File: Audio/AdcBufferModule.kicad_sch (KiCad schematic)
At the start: 13 parts

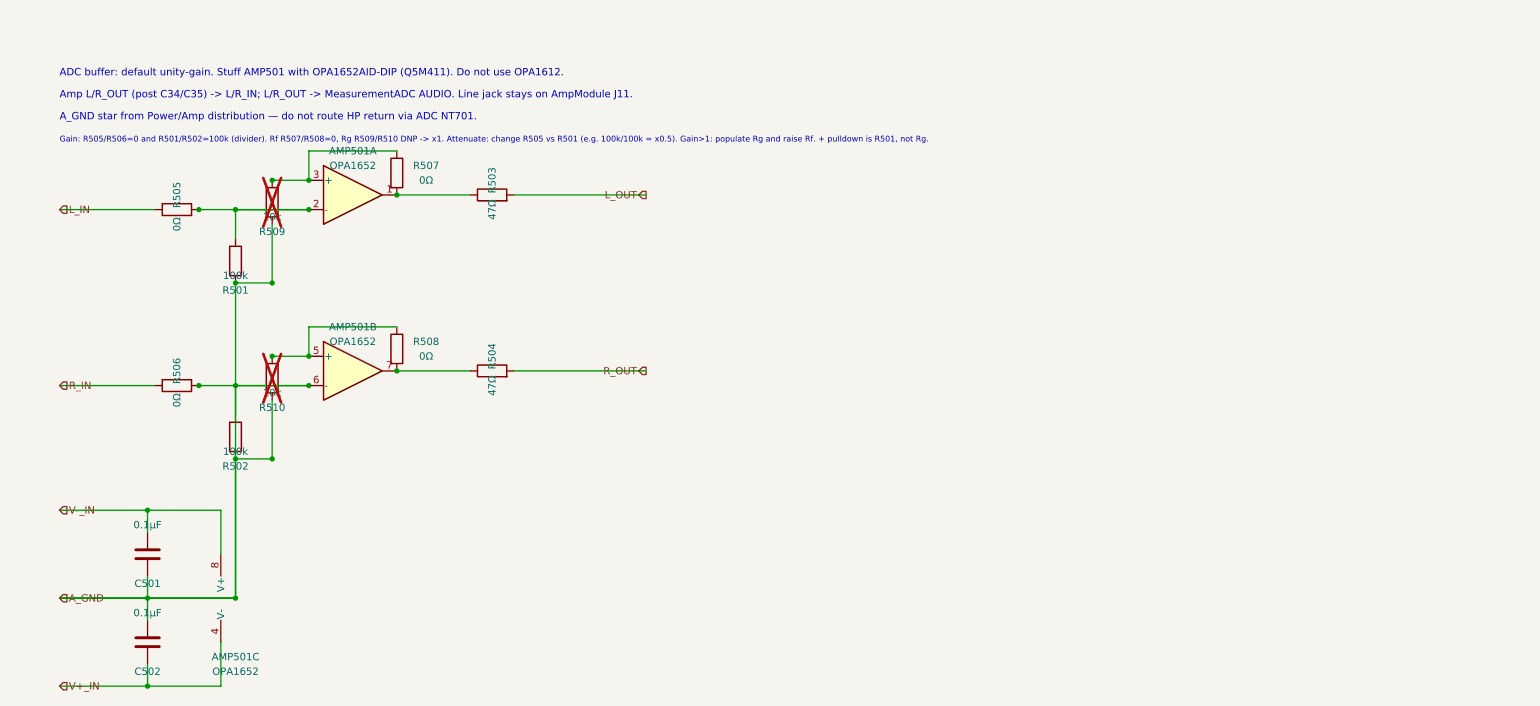
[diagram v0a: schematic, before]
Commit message: ヘッドホン出力と切替を追加し、S式検査をコミット前に走らせる。
Amp 後段を PHONE/MUTE/LINE に分け、NJM4556A の電流バッファとパッド付きボリュームを載せる。括弧崩れで回路図が開けなくなるのを check_sexpr と pre-commit で止める。

Co-authored-by: Cursor <cursoragent@cursor.com>
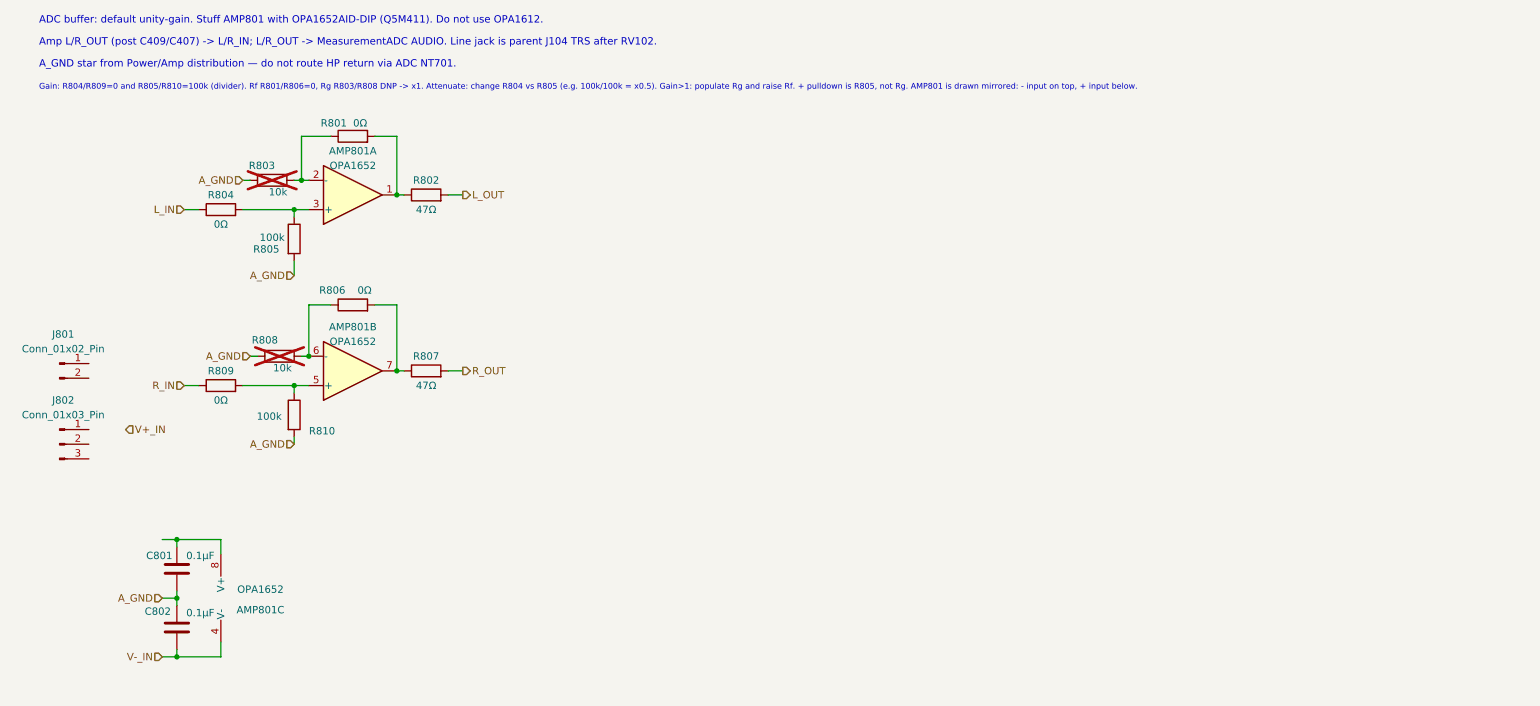
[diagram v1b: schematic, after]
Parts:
- added J801: Conn_01x02_Pin, symbol Connector:Conn_01x02_Pin
- added J802: Conn_01x03_Pin, symbol Connector:Conn_01x03_Pin
- renumbered AMP501 to AMP801, C501 to C801, C502 to C802, R507 to R801, R503 to R802, R509 to R803, R505 to R804, R501 to R805, R508 to R806, R504 to R807, R510 to R808, R506 to R809, R502 to R810
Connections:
- net A_GND: now also R803.1, R808.1; no longer AMP801.6 (-), R803.2, R808.2, R809.2, R810.1
- net V+_IN: no longer AMP801.4 (V-), C802.2
- net V-_IN: now also AMP801.4 (V-), C802.2; no longer AMP801.8 (V+), C801.1
- net at R804.2, R805.1: now also AMP801.3 (+); no longer AMP801.2 (-)
- new net: AMP801.5 (+), R809.2, R810.1
- new net: AMP801.6 (-), R806.1, R808.2
- new net: AMP801.8 (V+), C801.1
- new net: AMP801.2 (-), R801.1, R803.2
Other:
- note added: "ADC buffer: default unity-gain. Stuff AMP801 with OPA1652AID-DIP (Q5M411). Do not use OPA1612."
- note added: "Amp L/R_OUT (post C409/C407) -> L/R_IN; L/R_OUT -> MeasurementADC AUDIO. Line jack is parent J104 TRS after RV102."
- note added: "Gain: R804/R809=0 and R805/R810=100k (divider). Rf R801/R806=0, Rg R803/R808 DNP -> x1. Attenuate: change R804 vs R805 (e.g. 100k/100k = x0.5). Gain>1: populate Rg and raise Rf. + pulldown is R805, not Rg. AMP801 is drawn mirrored: - input on top, + input below."
- note removed: "ADC buffer: default unity-gain. Stuff AMP501 with OPA1652AID-DIP (Q5M411). Do not use OPA1612."
- note removed: "Amp L/R_OUT (post C34/C35) -> L/R_IN; L/R_OUT -> MeasurementADC AUDIO. Line jack stays on AmpModule J11."
- note removed: "Gain: R505/R506=0 and R501/R502=100k (divider). Rf R507/R508=0, Rg R509/R510 DNP -> x1. Attenuate: change R505 vs R501 (e.g. 100k/100k = x0.5). Gain>1: populate Rg and raise Rf. + pulldown is R501, not Rg."
- moved on the sheet: C801, C802, R801, R802, R803, R804, R805, R806, R807, R808, R809, R810
